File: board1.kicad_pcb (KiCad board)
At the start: 2 copper layers, 99.3 x 99.3 mm, 0 parts

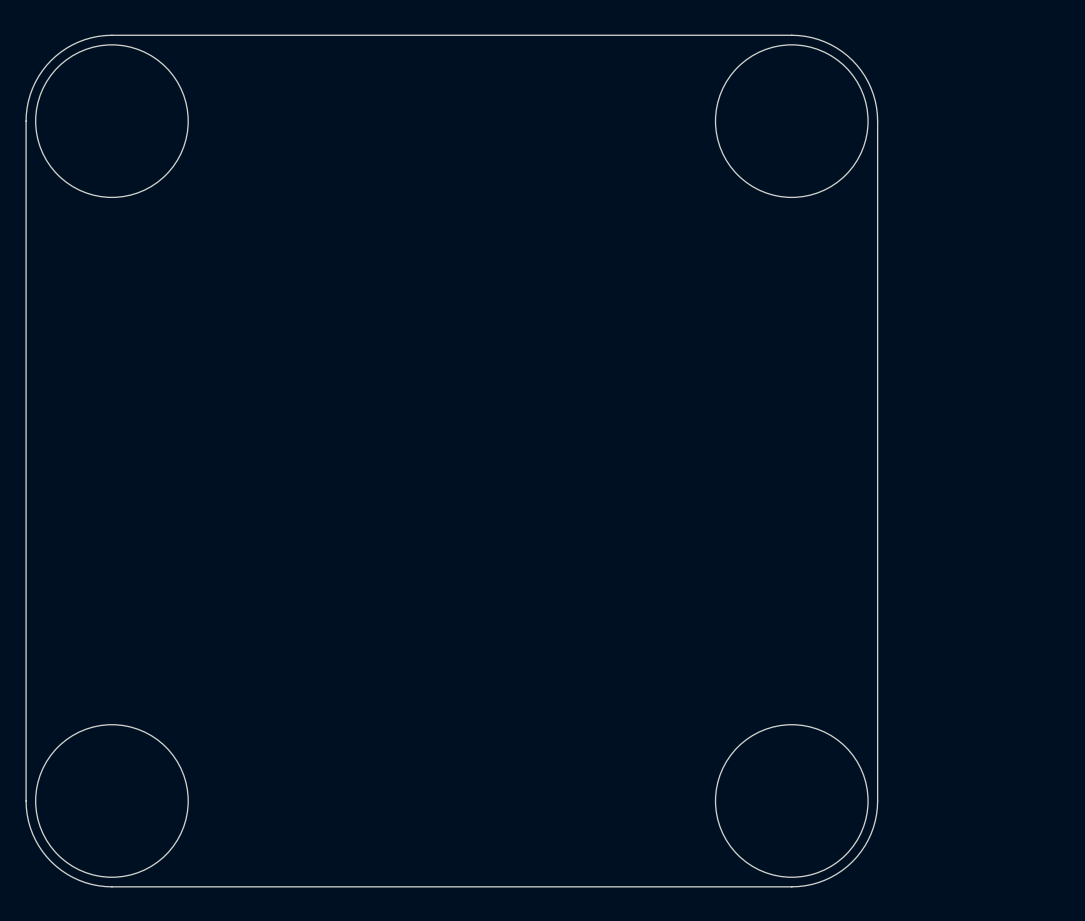
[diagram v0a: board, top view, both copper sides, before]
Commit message: Updated Edge Cuts
Updated edge cuts with updated dimensions
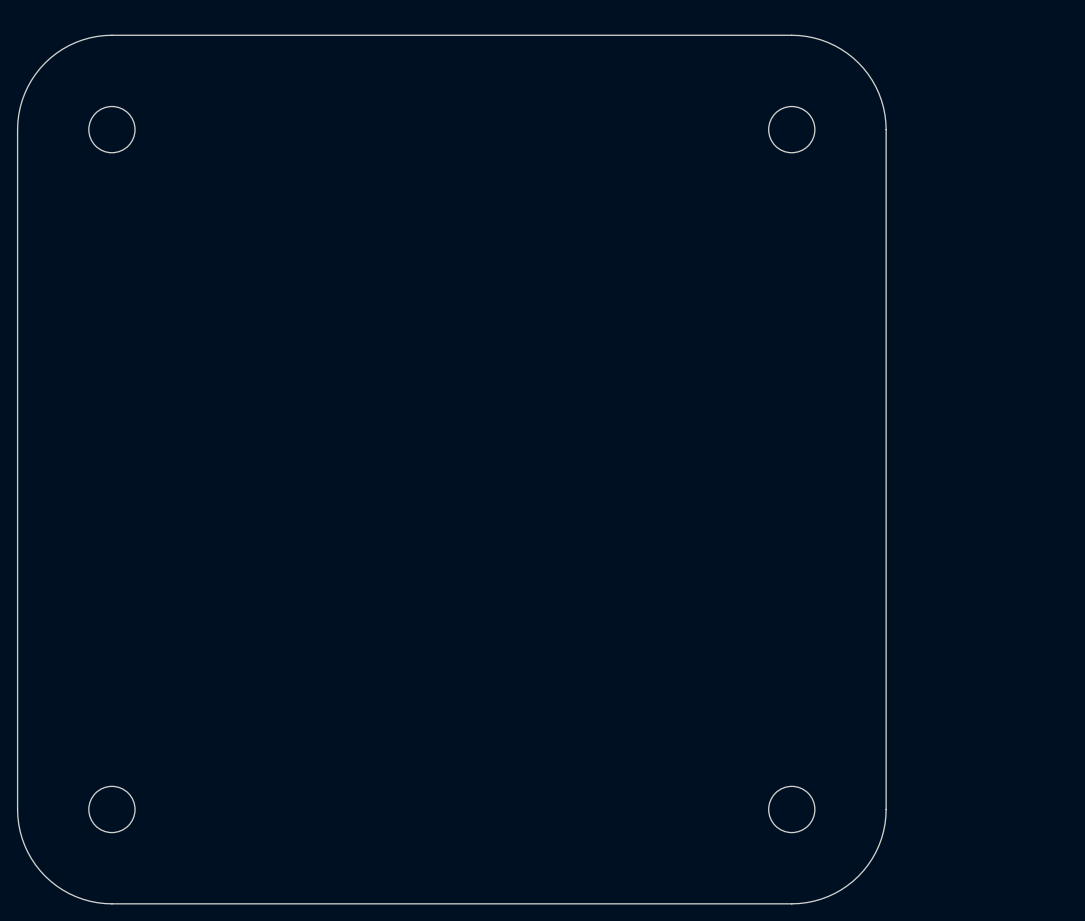
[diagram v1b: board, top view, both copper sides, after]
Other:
- board size 99.3 x 99.3 mm -> 101.2 x 101.2 mm
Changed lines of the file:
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@@
   )
   (net 0 "")
-  (gr_line (start 91.5924 70.0076) (end 91.5924 149.2556) (layer "Edge.Cuts") (width 0.1))
-  (gr_circle (center 101.6 70.0076) (end 110.49 70.0076) (layer "Edge.Cuts") (width 0.1) (fill none))
-  (gr_line (start 190.8556 70.0076) (end 190.8556 149.2556) (layer "Edge.Cuts") (width 0.1))
-  (gr_circle (center 101.6 149.2556) (end 110.49 149.2556) (layer "Edge.Cuts") (width 0.1) (fill none))
-  (gr_line (start 101.6 159.2632) (end 180.848 159.2632) (layer "Edge.Cuts") (width 0.1))
+  (gr_arc (start 180.848 60) (mid 188.624902 63.221298) (end 191.8462 70.9982) (layer "Edge.Cuts") (width 0.1))
+  (gr_line (start 90.6018 70.9982) (end 90.6018 150.2462) (layer "Edge.Cuts") (width 0.1))
+  (gr_circle (center 101.6 70.9982) (end 104.2924 70.9982) (layer "Edge.Cuts") (width 0.1) (fill none))
+  (gr_arc (start 101.6 161.2444) (mid 93.823098 158.023102) (end 90.6018 150.2462) (layer "Edge.Cuts") (width 0.1))
+  (gr_line (start 191.8462 70.9982) (end 191.8462 150.2462) (layer "Edge.Cuts") (width 0.1))
+  (gr_circle (center 101.6 150.2462) (end 104.2924 150.2462) (layer "Edge.Cuts") (width 0.1) (fill none))
+  (gr_line (start 101.6 161.2444) (end 180.848 161.2444) (layer "Edge.Cuts") (width 0.1))
   (gr_line (start 101.6 60) (end 180.848 60) (layer "Edge.Cuts") (width 0.1))
-  (gr_circle (center 180.848 149.2556) (end 189.738 149.2556) (layer "Edge.Cuts") (width 0.1) (fill none))
-  (gr_circle (center 180.848 70.0076) (end 189.738 70.0076) (layer "Edge.Cuts") (width 0.1) (fill none))
-  (gr_arc (start 190.8556 149.2556) (mid 187.924442 156.332042) (end 180.848 159.2632) (layer "Edge.Cuts") (width 0.1))
-  (gr_arc (start 101.6 159.2632) (mid 94.523558 156.332042) (end 91.5924 149.2556) (layer "Edge.Cuts") (width 0.1))
-  (gr_arc (start 180.848 60) (mid 187.924442 62.931158) (end 190.8556 70.0076) (layer "Edge.Cuts") (width 0.1))
-  (gr_arc (start 91.5924 70.0076) (mid 94.523558 62.931158) (end 101.6 60) (layer "Edge.Cuts") (width 0.1))
+  (gr_circle (center 180.848 150.2462) (end 183.5404 150.2462) (layer "Edge.Cuts") (width 0.1) (fill none))
+  (gr_arc (start 191.8462 150.2462) (mid 188.624902 158.023102) (end 180.848 161.2444) (layer "Edge.Cuts") (width 0.1))
+  (gr_arc (start 90.6018 70.9982) (mid 93.823098 63.221298) (end 101.6 60) (layer "Edge.Cuts") (width 0.1))
+  (gr_circle (center 180.848 70.9982) (end 183.5404 70.9982) (layer "Edge.Cuts") (width 0.1) (fill none))
   (gr_text "circles are arbitrary radius, can be resized for mounting holes later\ndo not edit for now, if need be, just change radius\n" (at 139 54) (layer "Edge.Cuts")
     (effects (font (size 1 1) (thickness 0.15)))

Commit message: stuff
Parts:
- added ENC_CONN1: Conn_01x06_Male, Connector_PinHeader_2.54mm:PinHeader_1x06_P2.54mm_Vertical, F.Cu at (100.0, 80.7)
- added ENC_CONN2: Conn_01x06_Male, Connector_PinSocket_2.54mm:PinSocket_1x06_P2.54mm_Vertical, F.Cu at (100.0, 100.7)
- added ENC_CONN3: Conn_01x06_Male, Connector_PinSocket_2.54mm:PinSocket_1x06_P2.54mm_Vertical, F.Cu at (110.7, 66.0)
- added ENC_CONN4: Conn_01x06_Male, Connector_PinSocket_2.54mm:PinSocket_1x06_P2.54mm_Vertical, F.Cu at (131.5, 66.0)
- added J6: XT30 Male Connector, Connector_AMASS:AMASS_XT30U-M_1x02_P5.0mm_Vertical, F.Cu at (186.0, 86.5)
- added MC1: DRV8876, board1_footprints:DRV8876, B.Cu at (171.0, 91.7)
- added MC2: DRV8876, board1_footprints:DRV8876, B.Cu at (150.0, 91.7)
- added MC3: DRV8876, board1_footprints:DRV8876, B.Cu at (171.0, 114.7)
- added MC4: DRV8876, board1_footprints:DRV8876, B.Cu at (150.0, 114.7)
- added R1: 4.7k, board1_footprints:Resistor, F.Cu at (167.0, 156.0)
- added R2: 4.7k, board1_footprints:Resistor, F.Cu at (167.0, 151.0)
- added R3: 0 Ohms, board1_footprints:Resistor, F.Cu at (142.0, 86.0)
- added TOF_STEMMA_QT1: Conn_01x04_Female, board1_footprints:Stemma QT, F.Cu at (109.8, 154.2)
- added TOF_STEMMA_QT2: Conn_01x04_Female, board1_footprints:Stemma QT, F.Cu at (123.0, 154.2)
- added TOF_STEMMA_QT3: Conn_01x04_Female, board1_footprints:Stemma QT, F.Cu at (136.1, 154.3)
- added TOF_STEMMA_QT4: Conn_01x04_Female, board1_footprints:Stemma QT, F.Cu at (149.6, 154.3)
- added TOF_XSHUT1: Conn_01x02_Female, Connector_PinSocket_2.54mm:PinSocket_1x02_P2.54mm_Vertical, F.Cu at (111.5, 140.7)
- added TOF_XSHUT2: Conn_01x02_Female, Connector_PinSocket_2.54mm:PinSocket_1x02_P2.54mm_Vertical, F.Cu at (123.8, 140.7)
- added TOF_XSHUT3: Conn_01x02_Female, Connector_PinSocket_2.54mm:PinSocket_1x02_P2.54mm_Vertical, F.Cu at (136.0, 140.8)
- added TOF_XSHUT4: Conn_01x02_Female, Connector_PinSocket_2.54mm:PinSocket_1x02_P2.54mm_Vertical, F.Cu at (147.0, 140.7)
- added U1: BNO085, board1_footprints:BNU0085, F.Cu at (159.0, 68.6)
- added U2: Teensy_4.0, board1_footprints:Teensy 4.0, F.Cu at (123.0, 78.8)
- added U3: Raspberry_PI_Zero_W, Connector_PinHeader_2.54mm:PinHeader_2x20_P2.54mm_Vertical, F.Cu at (183.7, 94.9)
- added U4: D24V50F5, board1_footprints:Voltage Regulator D24V50F5, F.Cu at (96.0, 132.0)

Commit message: Updated Footprints
Updated Footprints to indicate physical limitations of components
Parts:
- U3: footprint Connector_PinHeader_2.54mm:PinHeader_2x20_P2.54mm_Vertical -> board1_footprints:Raspberry Pi Zero W
- moved J6 8.25 mm to (178.0, 84.5)
- moved U3 5.64 mm to (186.2, 89.8)
- moved U4 5.49 mm to (93.8, 127.0), turned to 0 degrees

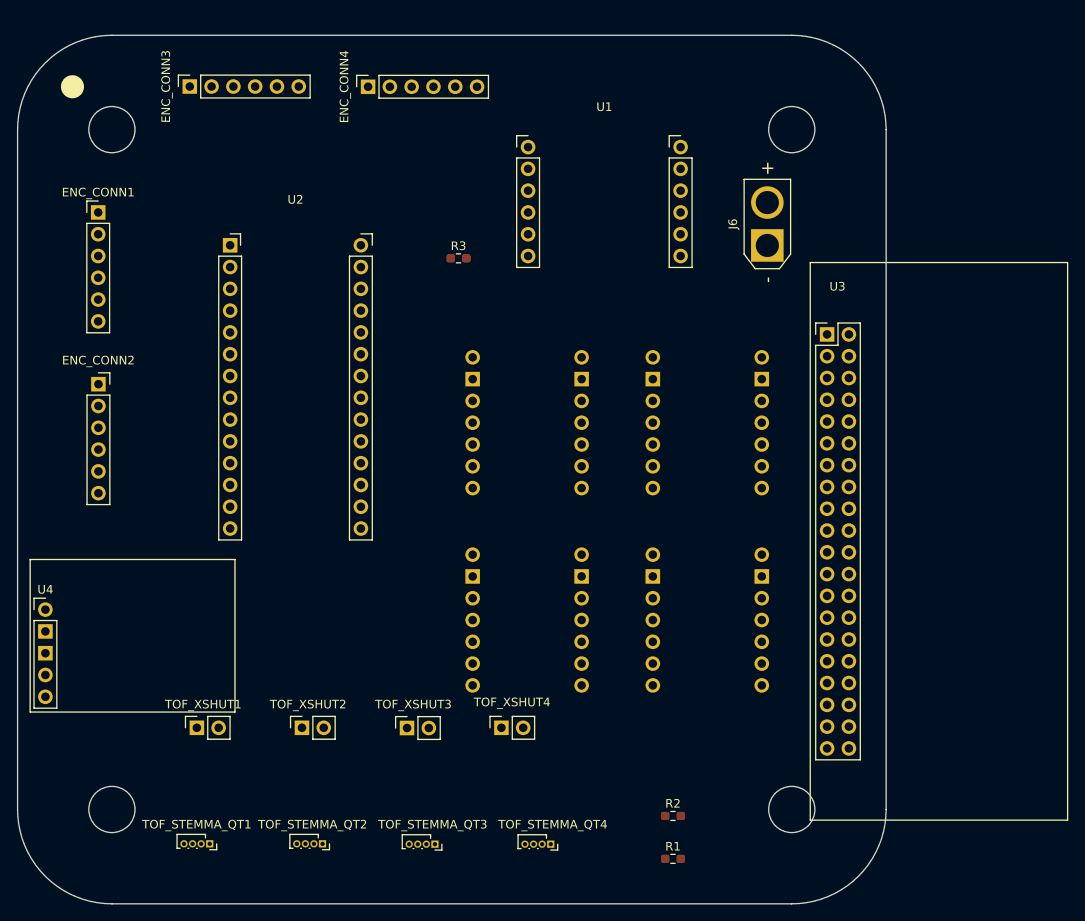
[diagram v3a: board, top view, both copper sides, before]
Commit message: updated board pcb to better match physical constraints
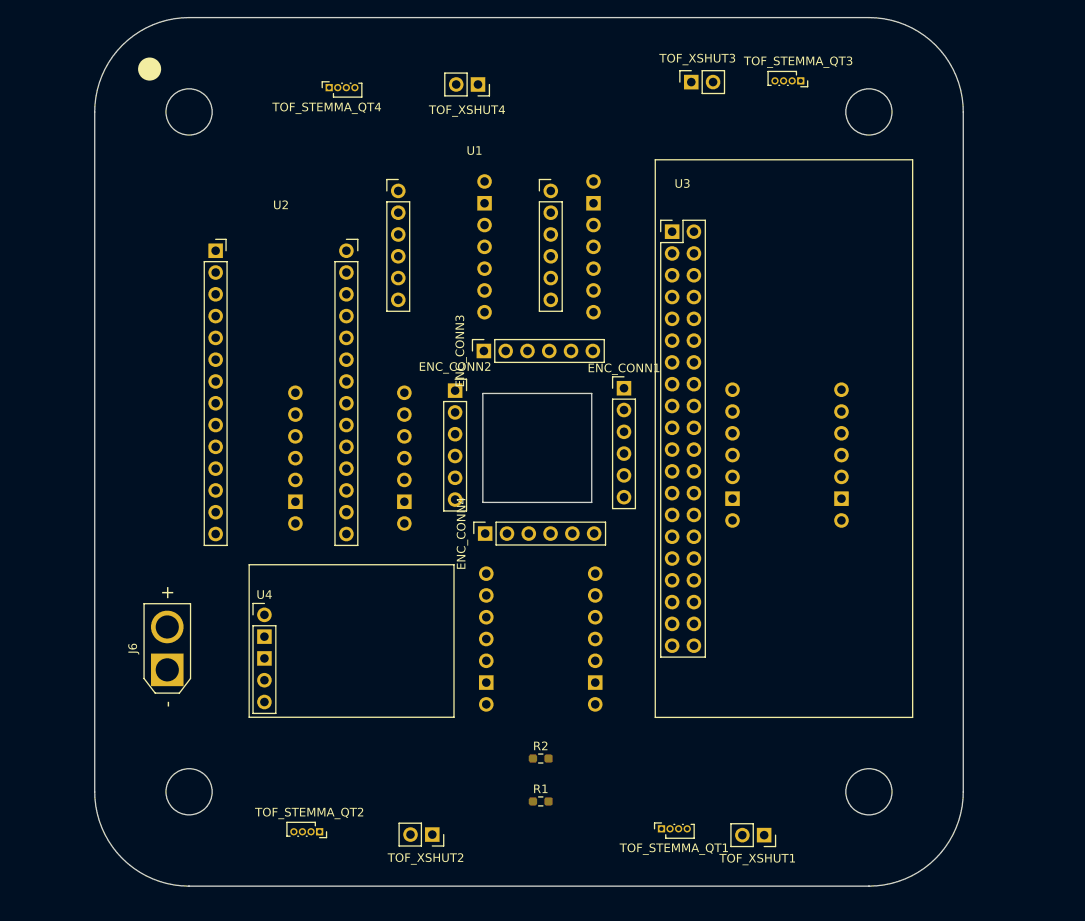
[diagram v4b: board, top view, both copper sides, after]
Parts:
- removed R3: 0 Ohms, board1_footprints:Resistor
- moved TOF_STEMMA_QT3 98.7 mm to (178.7, 65.3)
- moved TOF_STEMMA_QT4 90.3 mm to (130.1, 66.1), turned to -90 degrees
- moved J6 85.7 mm to (108.1, 134.0)
- moved TOF_XSHUT3 82.3 mm to (169.1, 65.5)
- moved TOF_XSHUT4 75.0 mm to (144.3, 65.7), turned to -90 degrees
- moved TOF_XSHUT1 67.3 mm to (177.6, 153.2), turned to -90 degrees
- moved ENC_CONN1 64.6 mm to (161.3, 101.1)
- moved TOF_STEMMA_QT1 59.0 mm to (168.8, 152.5), turned to -90 degrees
- moved ENC_CONN4 53.8 mm to (145.1, 118.1)
- moved MC2 52.2 mm to (151.6, 143.9), turned to 0 degrees
- moved MC1 52.0 mm to (129.3, 122.8), turned to 0 degrees
- moved MC3 47.7 mm to (151.4, 71.2)
- moved ENC_CONN3 46.1 mm to (145.0, 96.8)
- moved ENC_CONN2 41.6 mm to (141.6, 101.4)
- moved MC4 31.3 mm to (180.3, 122.4), turned to 0 degrees
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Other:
- outline, holes or cut-outs redrawn

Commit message: slight edits
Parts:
- added R3: 0 Ohms, board1_footprints:Resistor, F.Cu at (103.1, 97.0)
- moved ENC_CONN2 13.6 mm to (141.6, 115.0), turned to 180 degrees
- moved ENC_CONN4 13.2 mm to (158.3, 118.1), turned to -90 degrees
- moved TOF_STEMMA_QT3 4.91 mm to (183.7, 65.3), turned to -90 degrees
- moved J6 4.47 mm to (108.0, 129.5), turned to -90 degrees
- moved TOF_STEMMA_QT1 4.46 mm to (164.3, 152.5), turned to 90 degrees
- moved U3 2.90 mm to (171.0, 78.0)
- moved TOF_XSHUT3 1.46 mm to (169.0, 64.0)
- moved ENC_CONN3 0.18 mm to (145.0, 97.0)

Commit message: made changes
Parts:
- TOF_STEMMA_QT1, TOF_STEMMA_QT2, TOF_STEMMA_QT3, TOF_STEMMA_QT4: footprint board1_footprints:Stemma QT -> Connector_JST:JST_SH_BM04B-SRSS-TB_1x04-1MP_P1.00mm_Vertical
- U1: footprint board1_footprints:BNU0085 -> Connector_JST:JST_SH_BM04B-SRSS-TB_1x04-1MP_P1.00mm_Vertical
- moved U1 26.7 mm to (119.0, 64.0)
- moved TOF_STEMMA_QT3 2.96 mm to (181.0, 64.0), turned to 0 degrees
- moved TOF_STEMMA_QT2 2.35 mm to (125.0, 153.0), turned to 180 degrees
- moved TOF_STEMMA_QT4 1.11 mm to (130.0, 65.0), turned to 0 degrees
- turned TOF_STEMMA_QT1 to 180 degrees
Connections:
- MC1 pad 5: /5V -> GNDREF
- MC1 pad 6: /5V -> /3V3_Teensy
- MC2 pad 5: /5V -> GNDREF
- MC2 pad 6: /5V -> /3V3_Teensy
- MC3 pad 5: /5V -> GNDREF
- MC3 pad 6: /5V -> /3V3_Teensy
- MC4 pad 5: /5V -> GNDREF
- MC4 pad 6: /5V -> /3V3_Teensy
- R1 pad 2: /3V3 RPI -> /3V3_Teensy
- R2 pad 2: /3V3 RPI -> /3V3_Teensy
- TOF_STEMMA_QT1 pad 2: /3V3 RPI -> /3V3_Teensy
- TOF_STEMMA_QT2 pad 2: /3V3 RPI -> /3V3_Teensy
- TOF_STEMMA_QT3 pad 2: /3V3 RPI -> /3V3_Teensy
- TOF_STEMMA_QT4 pad 2: /3V3 RPI -> /3V3_Teensy
- U1 pad 1: unconnected-(U1-Pad1) -> GNDREF
- U1 pad 2: unconnected-(U1-Pad2) -> /3V3_Teensy
- U1 pad 3: unconnected-(U1-Pad3) -> /SDA_LINE
- U1 pad 4: unconnected-(U1-Pad4) -> /SCL_LINE
- U2 pad 10: /MC4_PWM2 -> /ENC_4_PINA
- U2 pad 11: /MC2_PWM1 -> /ENC_3_PINA
- U2 pad 12: /ENC_1_PINA -> /UART TXD (R PI)
- U2 pad 13: /MC2_PWM2 -> /MC1_PWM1
- U2 pad 14: /ENC_1_PINB -> /UART RXD (R PI)
- U2 pad 15: /MC3_PWM1 -> /MC1_PWM2
- U2 pad 16: /ENC_2_PINA -> /SCL_LINE
- U2 pad 17: unconnected-(U2-Pad17) -> /ENC_3_PINB
- U2 pad 18: /ENC_2_PINB -> /SDA_LINE
- U2 pad 19: unconnected-(U2-Pad19) -> /MC2_PWM1
- U2 pad 20: /ENC_3_PINA -> /ENC_4_PINB
- U2 pad 21: /MC3_PWM2 -> /MC2_PWM2
- U2 pad 22: /ENC_3_PINB -> /TOF_1_XSHUT
- U2 pad 23: unconnected-(U2-Pad23) -> /MC3_PWM1
- U2 pad 24: /ENC_4_PINA -> /TOF_2_XSHUT
- U2 pad 25: unconnected-(U2-Pad25) -> /MC3_PWM2
- U2 pad 26: /ENC_4_PINB -> /TOF_3_XSHUT
- U2 pad 27: unconnected-(U2-Pad27) -> /MC4_PWM1
- U2 pad 28: unconnected-(U2-Pad28) -> /TOF_4_XSHUT
- U2 pad 3: /UART TXD (R PI) -> /ENC_1_PINA
- U2 pad 5: /UART RXD (R PI) -> /ENC_1_PINB
- U2 pad 7: /MC1_PWM1 -> /ENC_2_PINA
- U2 pad 8: /MC4_PWM1 -> /MC4_PWM2
- U2 pad 9: /MC1_PWM2 -> /ENC_2_PINB
- U3 pad 25: GNDREF -> unconnected-(U3-Pad25)
- U3 pad 29: /TOF_1_XSHUT -> unconnected-(U3-Pad29)
- U3 pad 3: /SDA_LINE -> unconnected-(U3-Pad3)
- U3 pad 31: /TOF_2_XSHUT -> unconnected-(U3-Pad31)
- U3 pad 36: /TOF_3_XSHUT -> unconnected-(U3-Pad36)
- U3 pad 38: /TOF_4_XSHUT -> unconnected-(U3-Pad38)
- U3 pad 5: /SCL_LINE -> unconnected-(U3-Pad5)

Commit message: preliminary routing of traces
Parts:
- moved U2 43.7 mm to (119.0, 123.0), turned to 180 degrees
- moved MC1 27.3 mm to (126.0, 95.7), turned to 180 degrees
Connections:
- U2 pad 4: unconnected-(U2-Pad4) -> GNDREF
- U3 pad 14: unconnected-(U3-Pad14) -> GNDREF
- U3 pad 20: unconnected-(U3-Pad20) -> GNDREF
- U3 pad 25: unconnected-(U3-Pad25) -> GNDREF
- U3 pad 30: unconnected-(U3-Pad30) -> GNDREF
- U3 pad 34: unconnected-(U3-Pad34) -> GNDREF
- U3 pad 39: unconnected-(U3-Pad39) -> GNDREF
- U3 pad 4: unconnected-(U3-Pad4) -> /5V
- U3 pad 9: unconnected-(U3-Pad9) -> GNDREF
- U4 pad 3: unconnected-(U4-Pad3) -> /BATTERY_GROUND
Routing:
- net GNDREF: track 0.00 -> 488.3 mm, vias 0 -> 11
- net /3V3_Teensy: track 0.00 -> 342.8 mm, vias 0 -> 18
- net /SCL_LINE: track 0.00 -> 257.0 mm, vias 0 -> 4
- net /12V: track 0.00 -> 221.6 mm, vias 0 -> 2
- net /BATTERY_GROUND: track 0.00 -> 216.9 mm, vias 0 -> 5
- net /SDA_LINE: track 0.00 -> 216.5 mm, vias 0 -> 9
- net /5V: track 0.00 -> 127.9 mm, vias 0 -> 3
- net /TOF_1_XSHUT: track 0.00 -> 121.3 mm
- net /UART TXD (R PI): track 0.00 -> 109.7 mm, vias 0 -> 1
- net /UART RXD (R PI): track 0.00 -> 93.4 mm, vias 0 -> 2
- net /ENC_4_PINB: track 0.00 -> 87.8 mm, vias 0 -> 2
- net /MOTOR_1_PIN1: track 0.00 -> 79.0 mm, vias 0 -> 3
- net /TOF_2_XSHUT: track 0.00 -> 76.4 mm
- net /MC4_PWM2: track 0.00 -> 71.2 mm, vias 0 -> 3
- net /TOF_3_XSHUT: track 0.00 -> 71.0 mm
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
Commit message: Routed PCB
routed pcb
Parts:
- moved R3 70.1 mm to (145.9, 152.5), turned to -90 degrees
- moved MC1 26.7 mm to (126.2, 122.4), turned to 0 degrees
- moved MC4 22.6 mm to (180.3, 99.8), turned to 180 degrees
- moved ENC_CONN1 20.8 mm to (140.5, 102.0)
- moved ENC_CONN4 16.6 mm to (161.3, 101.8), turned to 0 degrees
- moved ENC_CONN2 16.4 mm to (157.6, 118.4), turned to -90 degrees
- moved TOF_XSHUT3 7.01 mm to (162.0, 63.7)
- moved R2 6.32 mm to (151.0, 150.6)
- moved TOF_XSHUT4 4.92 mm to (148.7, 63.6)
- moved R1 4.25 mm to (151.0, 153.5)
- moved MC2 2.50 mm to (152.0, 146.3)
- moved MC3 1.50 mm to (151.4, 69.7)
- moved J6 0.70 mm to (108.0, 130.2)
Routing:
- net GNDREF: track 488.3 -> 0.00 mm, vias 11 -> 0
- net /BATTERY_GROUND: track 216.9 -> 0.00 mm, vias 5 -> 0
- net /MC4_PWM2: track 71.2 -> 155.4 mm, vias 3 -> 5
- net /MOTOR_1_PIN1: track 79.0 -> 10.5 mm, vias 3 -> 0
- net /UART RXD (R PI): track 93.4 -> 160.1 mm, vias 2 -> 6
- net /MC4_PWM1: track 61.1 -> 123.5 mm, vias 0 -> 3
- net /3V3_Teensy: track 342.8 -> 392.4 mm, vias 18 -> 9
- net /UART TXD (R PI): track 109.7 -> 157.9 mm, vias 1 -> 6
- net /ENC_4_PINA: track 43.9 -> 89.2 mm, vias 0 -> 3
- net /MC3_PWM1: track 34.3 -> 69.3 mm, vias 1 -> 0
- net /MOTOR_1_PIN2: track 47.8 -> 14.2 mm, vias 2 -> 0
- net /MOTOR_4_PIN1: track 45.5 -> 15.7 mm
- net /MC3_PWM2: track 37.7 -> 64.9 mm
- net /TOF_2_XSHUT: track 76.4 -> 102.3 mm, vias 0 -> 1
- net /SCL_LINE: track 257.0 -> 234.5 mm, vias 4 -> 9
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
